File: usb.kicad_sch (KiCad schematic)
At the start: 90 parts, among them J16 USB-C_GCT_USB4105-GF-A, J4 USB-C_GCT_USB4105-GF-A

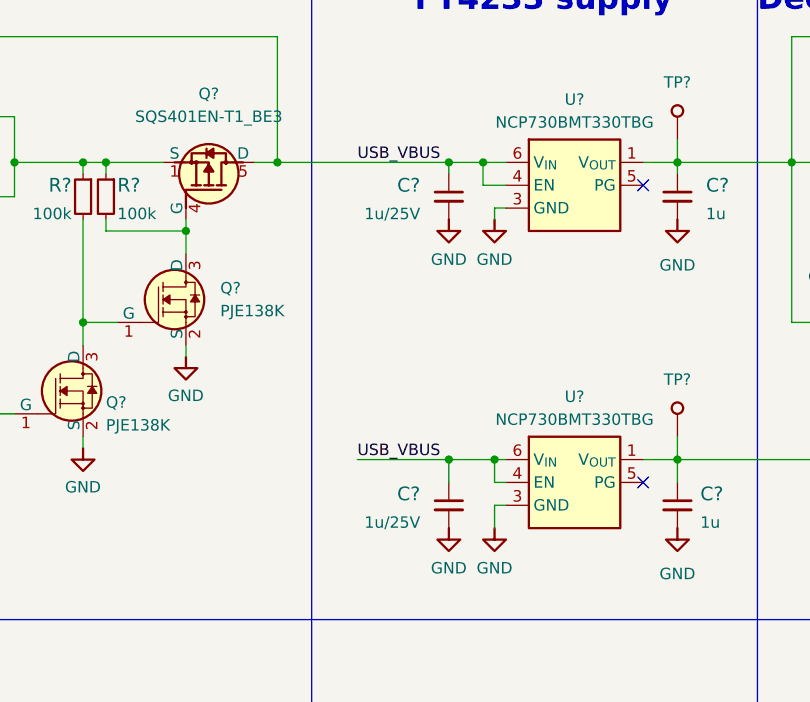
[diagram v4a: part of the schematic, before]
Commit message: [#54617] Reduce capacitors diversity
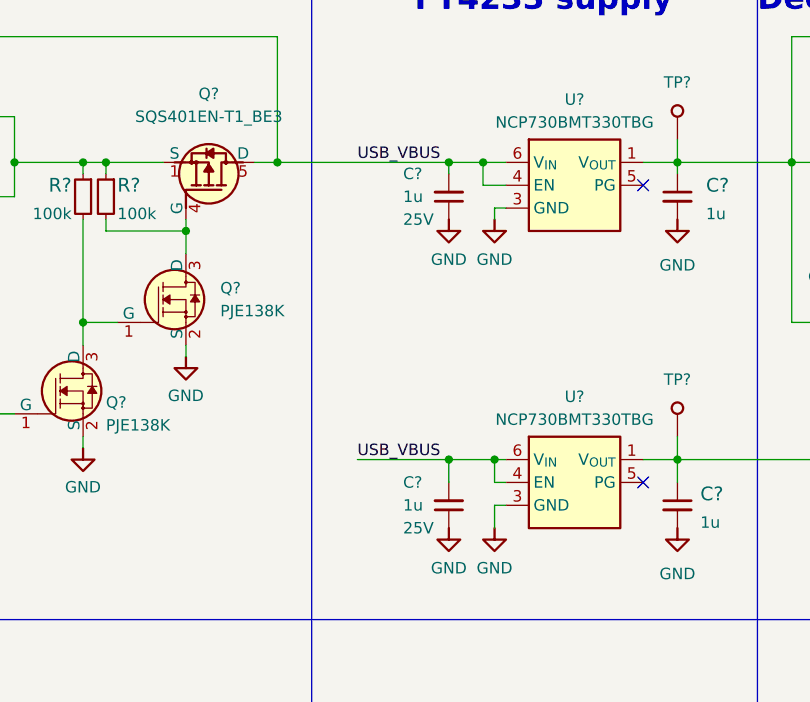
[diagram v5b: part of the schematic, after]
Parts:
- removed C? (x2): C_1u_25V_0603, antmicro-footprints:C_0603_1608Metric, symbol antmicroCapacitors0603:C_1u_25V_0603
- added C? (x2): C_1u_25V_0402, antmicro-footprints:C_0402_1005Metric, symbol antmicroCapacitors0402:C_1u_25V_0402
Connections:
- net GND: now also C?.1, C?.1
- net USB_VBUS: now also C?.2, C?.2
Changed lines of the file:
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@@
+    (pin "2")
+  )
+  (symbol (lib_id "antmicroCapacitors0402:C_1u_25V_0402") (at 224.79 151.13 90) (unit 1)
+    (in_bom yes) (on_board yes)
+    (property "Reference" "C?" (id 0) (at 219.71 146.05 90)
+      (effects (font (size 1.27 1.27) (thickness 0.15)) (justify right))
+    )
+    (property "Value" "C_1u_25V_0402" (id 1) (at 234.95 130.81 0)
+      (effects (font (size 1.27 1.27) (thickness 0.15)) (justify left bottom) hide)
+    )
+    (property "Footprint" "antmicro-footprints:C_0402_1005Metric" (id 2) (at 237.49 130.81 0)
+      (effects (font (size 1.27 1.27) (thickness 0.15)) (justify left bottom) hide)
+    )
+    (property "Datasheet" "https://www.murata.com/products/productdetail?partno=GRM155R61E105KE11%23" (id 3) (at 240.03 130.81 0)
+      (effects (font (size 1.27 1.27) (thickness 0.15)) (justify left bottom) hide)
+    )
+    (property "MPN" "GRM155R61E105KE11J" (id 4) (at 242.57 130.81 0)
+      (effects (font (size 1.27 1.27) (thickness 0.15)) (justify left bottom) hide)
+    )
+    (property "Manufacturer" "Murata" (id 5) (at 245.11 130.81 0)
+      (effects (font (size 1.27 1.27) (thickness 0.15)) (justify left bottom) hide)
+    )
+    (property "License" "Apache-2.0" (id 6) (at 247.65 130.81 0)
+      (effects (font (size 1.27 1.27) (thickness 0.15)) (justify left bottom) hide)
+    )
+    (property "Author" "Antmicro" (id 7) (at 250.19 130.81 0)
+      (effects (font (size 1.27 1.27) (thickness 0.15)) (justify left bottom) hide)
+    )
+    (property "Val" "1u" (id 8) (at 219.71 148.59 90)
+      (effects (font (size 1.27 1.27) (thickness 0.15)) (justify right))
+    )
+    (property "Voltage" "25V" (id 9) (at 219.71 151.13 90)
+      (effects (font (size 1.27 1.27)) (justify right))
+    )
+    (property "Dielectric" "X5R" (id 10) (at 255.27 130.81 0)
+      (effects (font (size 1.27 1.27)) (justify left bottom) hide)
+    )
+    (pin "1")
     (pin "2")
   )
@@
     (pin "7")
   )
-  (symbol (lib_id "antmicroCapacitors0603:C_1u_25V_0603") (at 224.79 146.05 270) (unit 1)
-    (in_bom yes) (on_board yes) (fields_autoplaced)
-    (property "Reference" "C?" (id 0) (at 221.615 147.3263 90)
-      (effects (font (size 1.524 1.524)) (justify right))
-    )
-    (property "Value" "C_1u_25V_0603" (id 1) (at 220.98 146.05 0)
-      (effects (font (size 1.27 1.27) (thickness 0.15)) (justify left bottom) hide)
-    )
-    (property "Footprint" "antmicro-footprints:C_0603_1608Metric" (id 2) (at 229.87 151.13 0)
-      (effects (font (size 1.27 1.27) (thickness 0.15)) (justify left bottom) hide)
-    )
-    (property "Datasheet" " " (id 3) (at 224.79 146.05 0)
-      (effects (font (size 1.27 1.27) (thickness 0.15)) (justify left bottom) hide)
-    )
-    (property "Manufacturer" "Samsung" (id 4) (at 234.95 151.13 0)
-      (effects (font (size 1.27 1.27) (thickness 0.15)) (justify left bottom) hide)
-    )
-    (property "MPN" "CL10A105KA8NNNC" (id 5) (at 232.41 151.13 0)
-      (effects (font (size 1.27 1.27) (thickness 0.15)) (justify left bottom) hide)
-    )
-    (property "Val" "1u/25V" (id 6) (at 221.615 150.5012 90)
-      (effects (font (size 1.27 1.27) (thickness 0.15)) (justify right))
-    )
-    (property "License" "Apache-2.0" (id 7) (at 201.93 166.37 0)
-      (effects (font (size 1.27 1.27) (thickness 0.15)) (justify left bottom) hide)
-    )
-    (property "Author" "Antmicro" (id 8) (at 199.39 166.37 0)
-      (effects (font (size 1.27 1.27) (thickness 0.15)) (justify left bottom) hide)
-    )
-    (property "Voltage" "" (id 9) (at 196.85 166.37 0)
-      (effects (font (size 1.27 1.27)) (justify left bottom) hide)
-    )
-    (property "Dielectric" "" (id 10) (at 194.31 166.37 0)
-      (effects (font (size 1.27 1.27)) (justify left bottom) hide)
-    )
-    (pin "1")
-    (pin "2")
-  )
   (symbol (lib_id "antmicroTransistorsFETsMOSFETsSingle:PJE138K") (at 128.27 149.86 0) (mirror y) (unit 1)
     (in_bom yes) (on_board yes)
@@
     )
     (pin "1")
+  )
+  (symbol (lib_id "antmicroCapacitors0402:C_1u_25V_0402") (at 224.79 116.84 90) (unit 1)
+    (in_bom yes) (on_board yes)
+    (property "Reference" "C?" (id 0) (at 219.71 111.76 90)
+      (effects (font (size 1.27 1.27) (thickness 0.15)) (justify right))
+    )
+    (property "Value" "C_1u_25V_0402" (id 1) (at 234.95 96.52 0)
+      (effects (font (size 1.27 1.27) (thickness 0.15)) (justify left bottom) hide)
+    )
+    (property "Footprint" "antmicro-footprints:C_0402_1005Metric" (id 2) (at 237.49 96.52 0)
+      (effects (font (size 1.27 1.27) (thickness 0.15)) (justify left bottom) hide)
+    )
+    (property "Datasheet" "https://www.murata.com/products/productdetail?partno=GRM155R61E105KE11%23" (id 3) (at 240.03 96.52 0)
+      (effects (font (size 1.27 1.27) (thickness 0.15)) (justify left bottom) hide)
+    )
+    (property "MPN" "GRM155R61E105KE11J" (id 4) (at 242.57 96.52 0)
+      (effects (font (size 1.27 1.27) (thickness 0.15)) (justify left bottom) hide)
+    )
+    (property "Manufacturer" "Murata" (id 5) (at 245.11 96.52 0)
+      (effects (font (size 1.27 1.27) (thickness 0.15)) (justify left bottom) hide)
+    )
+    (property "License" "Apache-2.0" (id 6) (at 247.65 96.52 0)
+      (effects (font (size 1.27 1.27) (thickness 0.15)) (justify left bottom) hide)
+    )
+    (property "Author" "Antmicro" (id 7) (at 250.19 96.52 0)
+      (effects (font (size 1.27 1.27) (thickness 0.15)) (justify left bottom) hide)
+    )
+    (property "Val" "1u" (id 8) (at 219.71 114.3 90)
+      (effects (font (size 1.27 1.27) (thickness 0.15)) (justify right))
+    )
+    (property "Voltage" "25V" (id 9) (at 219.71 116.84 90)
+      (effects (font (size 1.27 1.27)) (justify right))
+    )
+    (property "Dielectric" "X5R" (id 10) (at 255.27 96.52 0)
+      (effects (font (size 1.27 1.27)) (justify left bottom) hide)
+    )
+    (pin "1")
+    (pin "2")
   )
   (symbol (lib_id "antmicroCapacitors0402:C_18p_0402") (at 328.93 219.71 270) (unit 1)
@@
       (effects (font (size 1.27 1.27)) (justify left bottom) hide)
     )
-    (pin "1")
-    (pin "2")
-  )
-  (symbol (lib_id "antmicroCapacitors0603:C_1u_25V_0603") (at 224.79 111.76 270) (unit 1)
-    (in_bom yes) (on_board yes) (fields_autoplaced)
-    (property "Reference" "C?" (id 0) (at 221.615 113.0363 90)
-      (effects (font (size 1.524 1.524)) (justify right))
-    )
-    (property "Value" "C_1u_25V_0603" (id 1) (at 220.98 111.76 0)
-      (effects (font (size 1.27 1.27) (thickness 0.15)) (justify left bottom) hide)
-    )
-    (property "Footprint" "antmicro-footprints:C_0603_1608Metric" (id 2) (at 229.87 116.84 0)
-      (effects (font (size 1.27 1.27) (thickness 0.15)) (justify left bottom) hide)
-    )
-    (property "Datasheet" " " (id 3) (at 224.79 111.76 0)
-      (effects (font (size 1.27 1.27) (thickness 0.15)) (justify left bottom) hide)
-    )
-    (property "Manufacturer" "Samsung" (id 4) (at 234.95 116.84 0)
-      (effects (font (size 1.27 1.27) (thickness 0.15)) (justify left bottom) hide)
-    )
-    (property "MPN" "CL10A105KA8NNNC" (id 5) (at 232.41 116.84 0)
-      (effects (font (size 1.27 1.27) (thickness 0.15)) (justify left bottom) hide)
-    )
-    (property "Val" "1u/25V" (id 6) (at 221.615 116.2112 90)
-      (effects (font (size 1.27 1.27) (thickness 0.15)) (justify right))
-    )
-    (property "License" "Apache-2.0" (id 7) (at 201.93 132.08 0)
-      (effects (font (size 1.27 1.27) (thickness 0.15)) (justify left bottom) hide)
-    )
-    (property "Author" "Antmicro" (id 8) (at 199.39 132.08 0)
-      (effects (font (size 1.27 1.27) (thickness 0.15)) (justify left bottom) hide)
-    )
-    (property "Voltage" "" (id 9) (at 196.85 132.08 0)
-      (effects (font (size 1.27 1.27)) (justify left bottom) hide)
-    )
-    (property "Dielectric" "" (id 10) (at 194.31 132.08 0)
-      (effects (font (size 1.27 1.27)) (justify left bottom) hide)
-    )

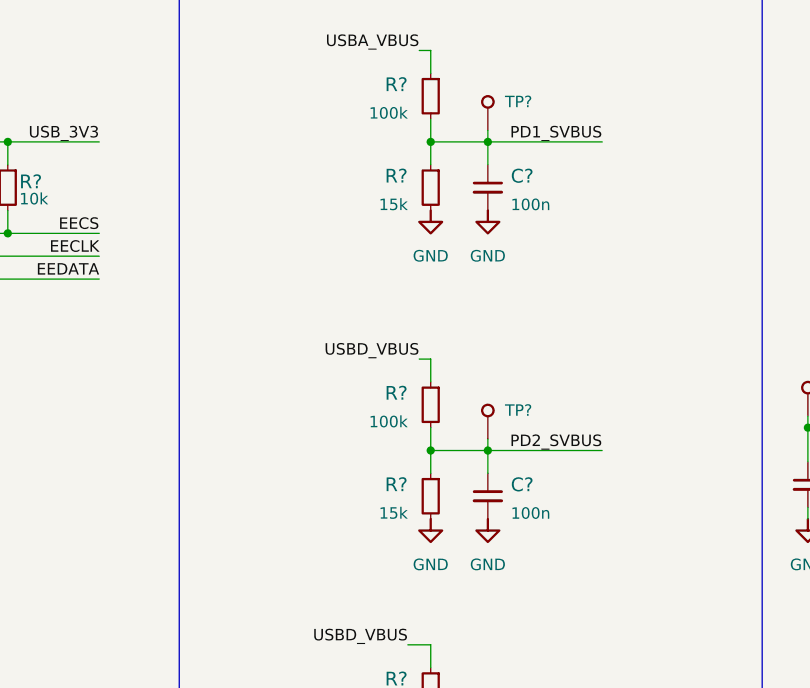
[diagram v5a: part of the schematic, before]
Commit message: [#54617] Reduce resistors diversity (switch size to 0402)
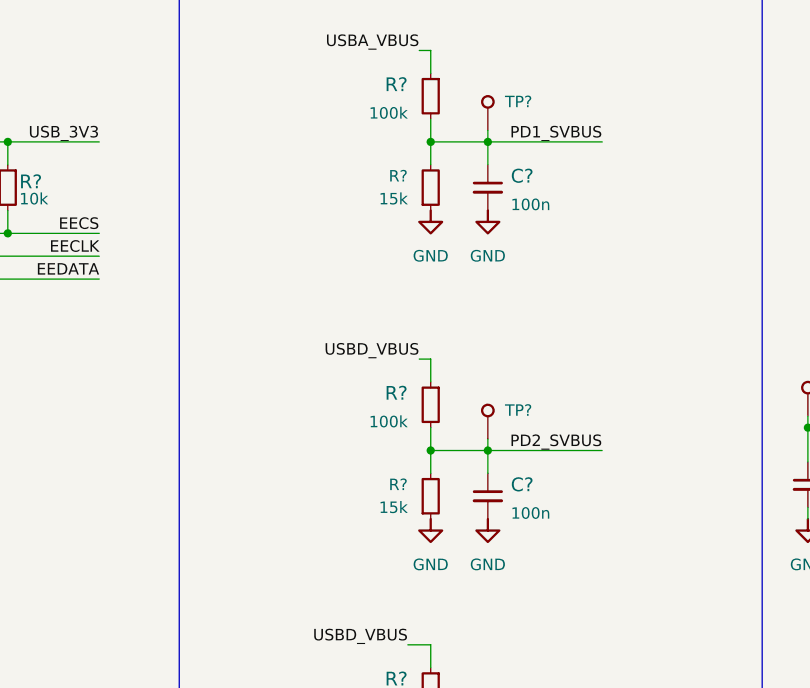
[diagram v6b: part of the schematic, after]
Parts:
- removed R? (x2): R_15k_0603, antmicro-footprints:R_0603_1608Metric, symbol antmicroResistors0603:R_15k_0603
- added R? (x2): R_15k_0402, antmicro-footprints:R_0402_1005Metric, symbol antmicroResistors0402:R_15k_0402
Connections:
- net GND: now also R?.1, R?.1
- net PD1_SVBUS: now also R?.2
- net PD2_SVBUS: now also R?.2
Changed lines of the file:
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@@
+    (pin "2")
+  )
+  (symbol (lib_id "antmicroResistors0402:R_15k_0402") (at 222.25 208.28 90) (unit 1)
+    (in_bom yes) (on_board yes) (fields_autoplaced)
+    (property "Reference" "R?" (id 0) (at 219.71 204.4699 90)
+      (effects (font (size 1.27 1.27)) (justify left))
+    )
+    (property "Value" "R_15k_0402" (id 1) (at 229.87 208.28 0)
+      (effects (font (size 1.27 1.27)) (justify left bottom) hide)
+    )
+    (property "Footprint" "antmicro-footprints:R_0402_1005Metric" (id 2) (at 217.17 203.2 0)
+      (effects (font (size 1.524 1.524)) (justify left bottom) hide)
+    )
+    (property "Datasheet" "https://www.bourns.com/docs/product-datasheets/cr.pdf" (id 3) (at 227.33 208.28 0)
+      (effects (font (size 1.27 1.27)) (justify left bottom) hide)
+    )
+    (property "Manufacturer" "Bourns" (id 4) (at 212.09 203.2 0)
+      (effects (font (size 1.524 1.524)) (justify left bottom) hide)
+    )
+    (property "MPN" "CR0402-FX-1502GLF" (id 5) (at 214.63 203.2 0)
+      (effects (font (size 1.524 1.524)) (justify left bottom) hide)
+    )
+    (property "Val" "15k" (id 6) (at 219.71 207.0099 90)
+      (effects (font (size 1.27 1.27)) (justify left))
+    )
+    (property "License" "Apache-2.0" (id 7) (at 247.65 187.96 0)
+      (effects (font (size 1.27 1.27) (thickness 0.15)) (justify left bottom) hide)
+    )
+    (property "Author" "Antmicro" (id 8) (at 250.19 187.96 0)
+      (effects (font (size 1.27 1.27) (thickness 0.15)) (justify left bottom) hide)
+    )
+    (property "Tolerance" "1%" (id 9) (at 232.41 187.96 0)
+      (effects (font (size 1.27 1.27)) (justify left bottom) hide)
+    )
+    (pin "1")
     (pin "2")
   )
@@
     (pin "2")
   )
-  (symbol (lib_id "antmicroResistors0603:R_15k_0603") (at 222.25 237.49 270) (unit 1)
-    (in_bom yes) (on_board yes) (fields_autoplaced)
-    (property "Reference" "R?" (id 0) (at 219.71 238.76 90)
-      (effects (font (size 1.524 1.524)) (justify right))
-    )
-    (property "Value" "R_15k_0603" (id 1) (at 218.44 237.49 0)
-      (effects (font (size 1.27 1.27) (thickness 0.15)) (justify left bottom) hide)
-    )
-    (property "Footprint" "antmicro-footprints:R_0603_1608Metric" (id 2) (at 227.33 242.57 0)
-      (effects (font (size 1.27 1.27) (thickness 0.15)) (justify left bottom) hide)
-    )
-    (property "Datasheet" "https://www.bourns.com/docs/product-datasheets/cr.pdf" (id 3) (at 222.25 237.49 0)
-      (effects (font (size 1.27 1.27) (thickness 0.15)) (justify left bottom) hide)
-    )
-    (property "Manufacturer" "Bourns" (id 4) (at 232.41 242.57 0)
-      (effects (font (size 1.27 1.27) (thickness 0.15)) (justify left bottom) hide)
-    )
-    (property "MPN" "CR0603-FX-1502ELF" (id 5) (at 229.87 242.57 0)
-      (effects (font (size 1.27 1.27) (thickness 0.15)) (justify left bottom) hide)
-    )
-    (property "Val" "15k" (id 6) (at 219.71 241.9349 90)
-      (effects (font (size 1.27 1.27) (thickness 0.15)) (justify right))
-    )
-    (property "License" "Apache-2.0" (id 7) (at 196.85 257.81 0)
-      (effects (font (size 1.27 1.27) (thickness 0.15)) (justify left bottom) hide)
-    )
-    (property "Author" "Antmicro" (id 8) (at 194.31 257.81 0)
-      (effects (font (size 1.27 1.27) (thickness 0.15)) (justify left bottom) hide)
-    )
-    (property "Tolerance" "1%" (id 9) (at 212.09 257.81 0)
+  (symbol (lib_id "antmicroResistors0402:R_15k_0402") (at 222.25 242.57 90) (unit 1)
+    (in_bom yes) (on_board yes) (fields_autoplaced)
+    (property "Reference" "R?" (id 0) (at 219.71 238.7599 90)
+      (effects (font (size 1.27 1.27)) (justify left))
+    )
+    (property "Value" "R_15k_0402" (id 1) (at 229.87 242.57 0)
+      (effects (font (size 1.27 1.27)) (justify left bottom) hide)
+    )
+    (property "Footprint" "antmicro-footprints:R_0402_1005Metric" (id 2) (at 217.17 237.49 0)
+      (effects (font (size 1.524 1.524)) (justify left bottom) hide)
+    )
+    (property "Datasheet" "https://www.bourns.com/docs/product-datasheets/cr.pdf" (id 3) (at 227.33 242.57 0)
+      (effects (font (size 1.27 1.27)) (justify left bottom) hide)
+    )
+    (property "Manufacturer" "Bourns" (id 4) (at 212.09 237.49 0)
+      (effects (font (size 1.524 1.524)) (justify left bottom) hide)
+    )
+    (property "MPN" "CR0402-FX-1502GLF" (id 5) (at 214.63 237.49 0)
+      (effects (font (size 1.524 1.524)) (justify left bottom) hide)
+    )
+    (property "Val" "15k" (id 6) (at 219.71 241.2999 90)
+      (effects (font (size 1.27 1.27)) (justify left))
+    )
+    (property "License" "Apache-2.0" (id 7) (at 247.65 222.25 0)
+      (effects (font (size 1.27 1.27) (thickness 0.15)) (justify left bottom) hide)
+    )
+    (property "Author" "Antmicro" (id 8) (at 250.19 222.25 0)
+      (effects (font (size 1.27 1.27) (thickness 0.15)) (justify left bottom) hide)
+    )
+    (property "Tolerance" "1%" (id 9) (at 232.41 222.25 0)
       (effects (font (size 1.27 1.27)) (justify left bottom) hide)
     )
@@
       (effects (font (size 1.27 1.27)) (justify left bottom) hide)
     )
-    (pin "1")
-    (pin "2")
-  )
-  (symbol (lib_id "antmicroResistors0603:R_15k_0603") (at 222.25 203.2 270) (unit 1)
-    (in_bom yes) (on_board yes) (fields_autoplaced)
-    (property "Reference" "R?" (id 0) (at 219.71 204.47 90)
-      (effects (font (size 1.524 1.524)) (justify right))
-    )
-    (property "Value" "R_15k_0603" (id 1) (at 218.44 203.2 0)
-      (effects (font (size 1.27 1.27) (thickness 0.15)) (justify left bottom) hide)
-    )
-    (property "Footprint" "antmicro-footprints:R_0603_1608Metric" (id 2) (at 227.33 208.28 0)
-      (effects (font (size 1.27 1.27) (thickness 0.15)) (justify left bottom) hide)
-    )
-    (property "Datasheet" "https://www.bourns.com/docs/product-datasheets/cr.pdf" (id 3) (at 222.25 203.2 0)
-      (effects (font (size 1.27 1.27) (thickness 0.15)) (justify left bottom) hide)
-    )
-    (property "Manufacturer" "Bourns" (id 4) (at 232.41 208.28 0)
-      (effects (font (size 1.27 1.27) (thickness 0.15)) (justify left bottom) hide)
-    )
-    (property "MPN" "CR0603-FX-1502ELF" (id 5) (at 229.87 208.28 0)
-      (effects (font (size 1.27 1.27) (thickness 0.15)) (justify left bottom) hide)
-    )
-    (property "Val" "15k" (id 6) (at 219.71 207.6449 90)
-      (effects (font (size 1.27 1.27) (thickness 0.15)) (justify right))
-    )
-    (property "License" "Apache-2.0" (id 7) (at 196.85 223.52 0)
-      (effects (font (size 1.27 1.27) (thickness 0.15)) (justify left bottom) hide)
-    )
-    (property "Author" "Antmicro" (id 8) (at 194.31 223.52 0)
-      (effects (font (size 1.27 1.27) (thickness 0.15)) (justify left bottom) hide)
-    )
-    (property "Tolerance" "1%" (id 9) (at 212.09 223.52 0)
-      (effects (font (size 1.27 1.27)) (justify left bottom) hide)
-    )
